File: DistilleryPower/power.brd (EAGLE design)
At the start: 50 x 86.9 mm, 68 parts, among them IC1 ACS758LCB-050B-PFF-T, IC3 MICROCHIP_BY_ELEMENT14_BATCH_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, IC4 SN65HVD230/1, J1 GREEN-2P-5.0, J2 GREEN-2P-5.0, J3 GREEN-2P-5.0, J4 GREEN-2P-5.0, J5 GREEN-2P-5.0, Q1 BC807-16LT1SMD, T1 BT138-DSH, U1 STM32F042KXTX, X1 IQD-FREQUENCY-PRODUCTS_CRYSTA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, X2 2516-

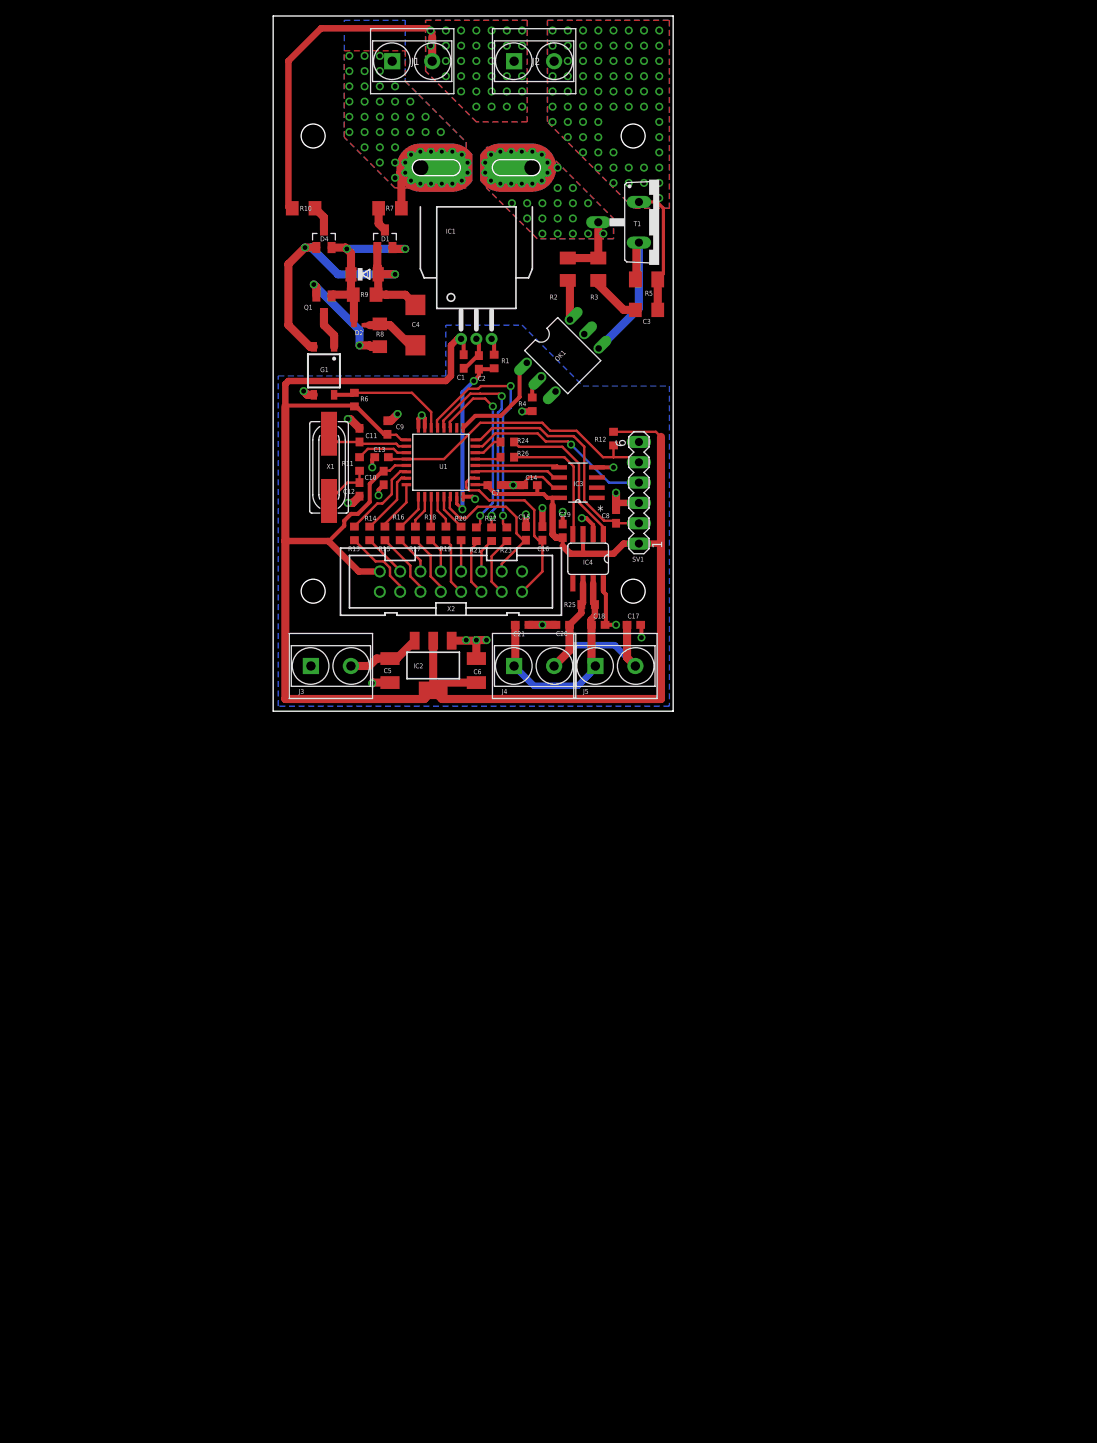
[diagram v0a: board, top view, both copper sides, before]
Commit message: reroute: indication board with CAN controller
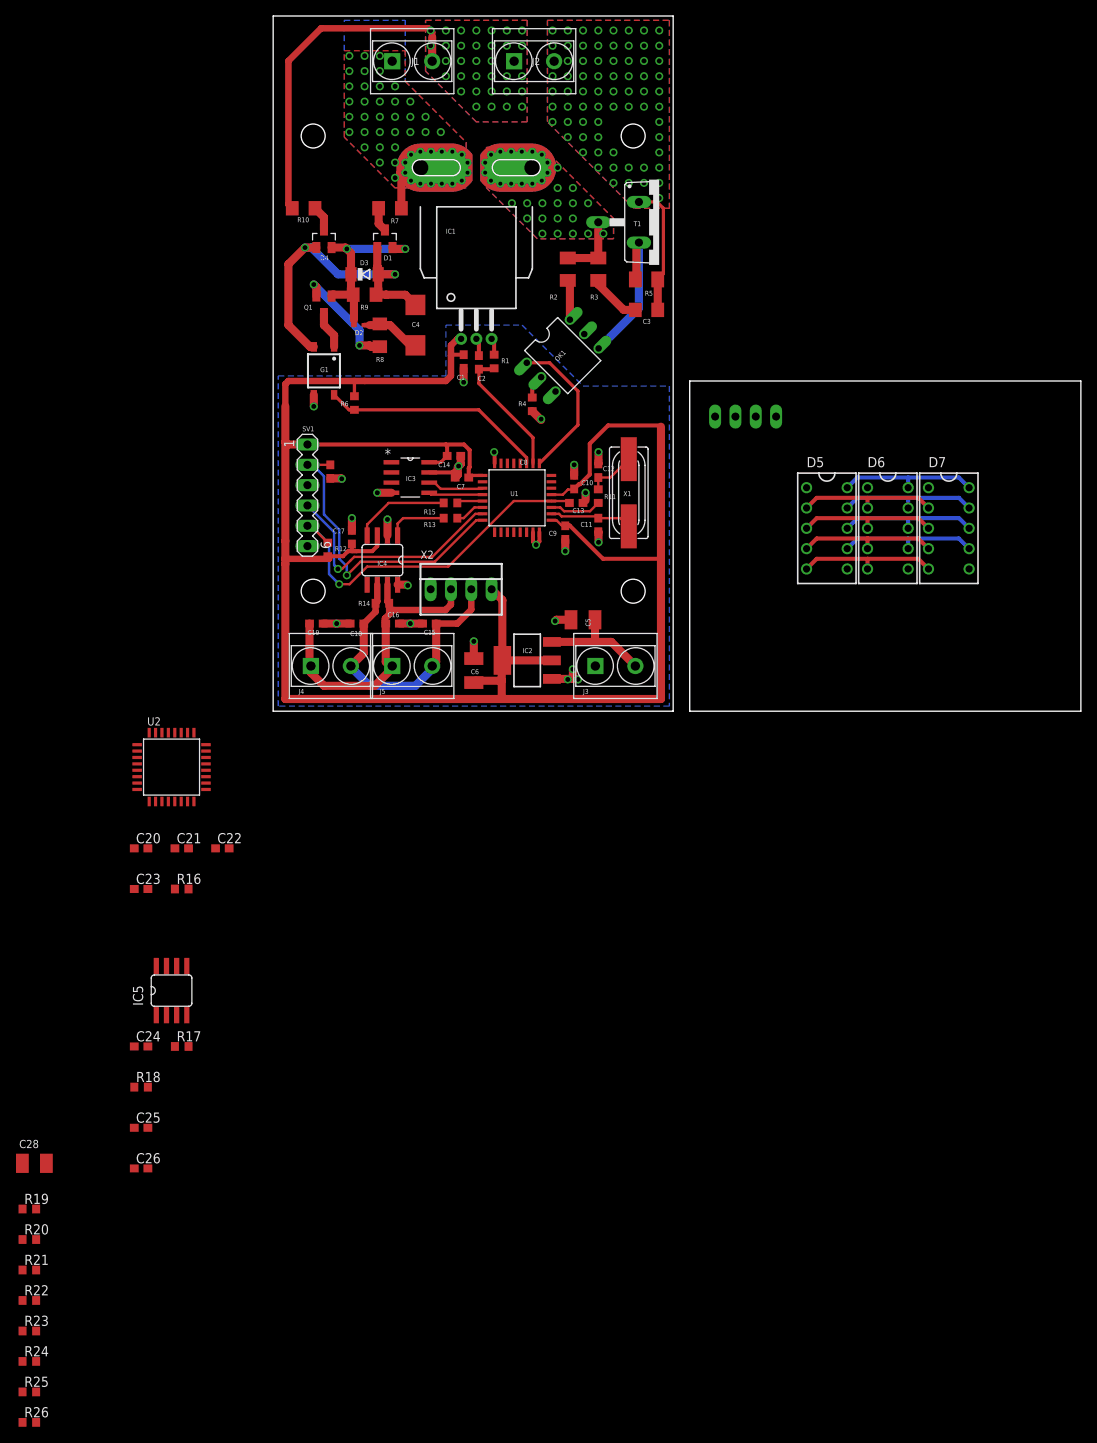
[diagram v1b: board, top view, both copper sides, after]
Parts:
- added C22, C23, C24, C25, C26: 0.1, rcl:C0603
- added C28: 10u/25, rcl:SMC_B
- added D5, D6, D7: CHRONO_LED_8X1, chrono:CHRONO_LED_DIP10
- added IC5: SN65HVD230/1, distillery:SO8
- added U2: STM32F042KXTX, stm32f0:LQFP32
- added X3: 22-23-2041, con-molex:22-23-2041
- R14: value 100 -> 120/1%
- R16, R19, R20, R21, R22, R23, R24, R26: value 100 -> (none)
- R25: value 120/1% -> (none)
- X2: value 2516- -> 22-23-2041; device con-3m:PAK100/2500-16 -> con-molex:22-23-2041
- moved R26 134.6 mm to (-30.5, -88.9), turned to 0 degrees
- moved R24 129.5 mm to (-30.5, -81.3), turned to 0 degrees
- moved R25 120.7 mm to (-30.5, -85.1)
- moved R23 116.1 mm to (-30.5, -77.5), turned to 0 degrees
- moved R22 111.9 mm to (-30.5, -73.7), turned to 0 degrees
- moved R21 107.6 mm to (-30.5, -69.8), turned to 0 degrees
- moved R20 103.5 mm to (-30.5, -66.0), turned to 0 degrees
- moved R19 99.2 mm to (-30.5, -62.2), turned to 0 degrees
- moved R18 78.1 mm to (-16.5, -47.0), turned to 0 degrees
- moved R17 70.5 mm to (-11.4, -41.9), turned to 0 degrees
- moved C20 59.7 mm to (-16.5, -17.1), turned to 0 degrees
- moved R16 52.2 mm to (-11.4, -22.2), turned to 0 degrees
- moved C21 50.9 mm to (-11.4, -17.1)
- moved SV1 41.4 mm to (4.29, 27.0), turned to 270 degrees
- moved R12 38.3 mm to (6.83, 20.2), turned to 270 degrees
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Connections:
- removed net DG0: R21.1, U1.27
- removed net DG1: R22.1, U1.28
- removed net DG2: R23.1, U1.29
- removed net N$33: R23.2, X2.13
- removed net SW0: C15.2, U1.14, X2.14
- removed net SW1: C16.2, U1.18, X2.15
- new net !I_NRST: C20.1, R16.1, U2.4
- new net I_3V3: C21.2, C22.2, C23.2, C24.2, C28.+, IC5.3, R16.2, U2.1, U2.17, U2.5, X3.4
- new net I_CAN_RX: R18.2, U2.21
- new net I_CAN_TX: R17.2, U2.22
- new net I_GND: C20.2, C21.1, C22.1, C23.1, C24.1, C25.2, C26.2, C28.-, IC5.2, IC5.8, U2.16, U2.31, U2.32, X3.1
- new net I_OSC_IN: U2.2
- new net I_OSC_OUT: U2.3
- new net LED_1: D5.1, D5.6
- new net LED_2: D6.1, D6.6
- new net LED_3: D7.1, D7.6
- new net N$12: C25.1, IC5.6, X3.3
- new net N$19: IC5.4, R18.1
- net +3V3: now also C17.2, X2.4; no longer C19.2, X2.2
- net A: now also D5.10, D6.10, D7.10, R19.1; no longer R13.1, U1.6
- net B: now also D5.9, D6.9, D7.9, R20.1; no longer R14.1, U1.7
- net C: now also D5.8, D6.8, D7.8, R21.1; no longer R15.1, U1.8
- net CAN_RX: now also R15.2; no longer R26.2
- net CAN_TX: now also R13.2; no longer R24.2
- net CUR_LOAD: now also U1.10; no longer U1.15
- net D: now also D5.5, D6.5, D7.5, R22.1; no longer R16.1, U1.9
- net DP: now also D5.7, D6.7, D7.7, R26.1; no longer R20.1, U1.13
- net E: now also D5.4, D6.4, D7.4, R23.1; no longer R17.1, U1.10
- net F: now also D5.2, D6.2, D7.2, R24.1; no longer R18.1, U1.11
- net G: now also D5.3, D6.3, D7.3, R25.1; no longer R19.1, U1.12
- net GND: now also C15.2, C16.2, C17.1, C19.2; no longer C15.1, C16.1, C17.2, C19.1, C20.2, C21.2, X2.16
- net N$15: now also IC5.1, R17.1; no longer R13.2, X2.3
- net N$20: now also C15.1, C18.1, R14.1, X2.3; no longer C17.1, C20.1, R25.1
- net N$21: now also R13.1; no longer R24.1
- net N$22: now also R15.1; no longer R26.1
- net N$23: now also C26.1, IC5.7, X3.2; no longer R14.2, X2.4
- net N$24: now also C16.1, C19.1, R14.2, X2.2; no longer C18.1, C21.1, R25.2
- net N$25: now also R19.2, U2.6; no longer R15.2, X2.5
- net N$26: now also R20.2, U2.7; no longer R16.2, X2.6
- net N$27: now also R21.2, U2.8; no longer R17.2, X2.7
- net N$28: now also R22.2, U2.9; no longer R18.2, X2.8
- net N$29: now also R23.2, U2.10; no longer R19.2, X2.9
- net N$30: now also R24.2, U2.11; no longer R20.2, X2.10
- net N$31: now also R25.2, U2.12; no longer R21.2, X2.11
- net N$32: now also R26.2, U2.13; no longer R22.2, X2.12
- net PHASE_OUT: now also U1.9; no longer U1.25
- net ZERO_CROSS: now also U1.11; no longer U1.30
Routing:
- net DG2: track 30.2 -> 0.00 mm, vias 2 -> 0
- net DG1: track 26.7 -> 0.00 mm, vias 2 -> 0
- net DG0: track 23.7 -> 0.00 mm, vias 2 -> 0
- net SW1: track 23.7 -> 0.00 mm
- net SW0: track 20.2 -> 0.00 mm
- net GND: track 66.2 -> 49.1 mm
- net F: track 3.77 -> 17.6 mm
- net G: track 4.17 -> 17.6 mm
- net E: track 4.23 -> 17.6 mm
- net DP: track 4.63 -> 17.6 mm
- net ZERO_CROSS: track 15.2 -> 28.0 mm
- net D: track 4.76 -> 17.6 mm
- net N$21: track 19.3 -> 7.53 mm
- net C: track 6.35 -> 17.6 mm
- net N$24: track 28.7 -> 39.5 mm
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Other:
- board size 50 x 86.9 mm -> 101 x 86.9 mm

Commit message: indication board routing finished
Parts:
- added C27: 100p, rcl:C0603
- added C29, C30: 20p, rcl:C0603
- added R27, R28, R29: 10k, rcl:R0603
- added R30: 220, rcl:R0603
- added S1, S2: SWITCH-TACT_DTS-6, chrono:SWITCH-TACT_DTS-6
- added SV2: (no value), distillery:CON-LSTB_MA06-1
- added VT1, VT2, VT3: WALKGEEK-EAGLE_IRLML6402, chrono:WALKGEEK-EAGLE_MICRO3
- added X4: IQD-FREQUENCY-PRODUCTS_CRYSTALS-NOGND-4-HSMX, distillery:IQD-FREQUENCY-PRODUCTS_HC49-4-HSMX
- moved R26 171.5 mm to (91.4, 31.8)
- moved R25 165.7 mm to (88.3, 30.5)
- moved R24 164.5 mm to (91.4, 29.2)
- moved R21 158.8 mm to (88.3, 35.6)
- moved R23 158.8 mm to (88.3, 27.9)
- moved R20 157.9 mm to (91.4, 34.3)
- moved R22 157.9 mm to (91.4, 26.7)
- moved R19 152.2 mm to (88.3, 33.0)
- moved C28 127.6 mm to (56.5, 37.5)
- moved C26 114.8 mm to (59.1, 29.2)
- moved C20 113.4 mm to (92.7, 13.3), turned to 180 degrees
- moved C25 112.9 mm to (59.1, 31.8)
- moved R16 109.4 mm to (92.7, 11.4), turned to 180 degrees
- moved R18 99.2 mm to (64.1, 10.8)
- moved C24 95.0 mm to (61.3, 12.5), turned to 180 degrees
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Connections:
- removed net LED_1: D5.1, D5.6
- removed net LED_2: D6.1, D6.6
- removed net LED_3: D7.1, D7.6
- new net AN_LED_1: D5.6, VT1.3
- new net AN_LED_2: D6.6, VT2.3
- new net AN_LED_3: D7.6, VT3.3
- new net BTN_1: S2.3, S2.4, U2.8
- new net BTN_2: S1.3, S1.4, U2.19
- new net I_SWCLK: C27.2, SV2.2, U2.24
- new net I_SWDIO: SV2.4, U2.23
- new net N$33: C30.2, R30.1, X4.2
- new net P_LED_1: R27.2, U2.28, VT1.1
- new net P_LED_2: R28.2, U2.29, VT2.1
- new net P_LED_3: R29.2, U2.30, VT3.1
- net !I_NRST: now also SV2.5
- net A: now also R21.1; no longer R19.1
- net B: now also R19.1; no longer R20.1
- net C: now also R25.1; no longer R21.1
- net DP: now also R23.1; no longer R26.1
- net E: now also R24.1; no longer R23.1
- net F: now also R20.1; no longer R24.1
- net G: now also R26.1; no longer R25.1
- net I_3V3: now also R27.1, R28.1, R29.1, SV2.1, VT1.2, VT2.2, VT3.2
- net I_GND: now also C27.1, C29.1, C30.1, S1.1, S1.2, S2.1, S2.2, SV2.3
- net I_OSC_IN: now also C29.2, X4.1
- net I_OSC_OUT: now also R30.2
- net N$25: now also U2.14; no longer U2.6
- net N$26: now also U2.15; no longer U2.7
- net N$27: now also U2.18; no longer U2.8
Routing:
- net I_3V3: track 0.00 -> 185.3 mm
- net I_SWDIO: track 0.00 -> 47.2 mm, vias 0 -> 2
- net N$27: track 0.00 -> 46.4 mm, vias 0 -> 2
- net I_SWCLK: track 0.00 -> 45.1 mm, vias 0 -> 2
- net N$26: track 0.00 -> 38.2 mm, vias 0 -> 2
- net N$25: track 0.00 -> 37.9 mm, vias 0 -> 2
- net N$31: track 0.00 -> 37.0 mm, vias 0 -> 2
- net I_GND: track 0.00 -> 35.4 mm, vias 0 -> 14
- net P_LED_3: track 0.00 -> 34.5 mm, vias 0 -> 2
- net N$32: track 0.00 -> 34.2 mm, vias 0 -> 2
- net BTN_1: track 0.00 -> 33.8 mm, vias 0 -> 2
- net N$29: track 0.00 -> 33.5 mm, vias 0 -> 2
- net N$30: track 0.00 -> 33.4 mm, vias 0 -> 2
- net !I_NRST: track 0.00 -> 32.5 mm, vias 0 -> 1
- net N$12: track 0.00 -> 30.7 mm, vias 0 -> 1
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- added copper zone on layer 16, net I_GND
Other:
- board size 101 x 86.9 mm -> 99.1 x 86.9 mm

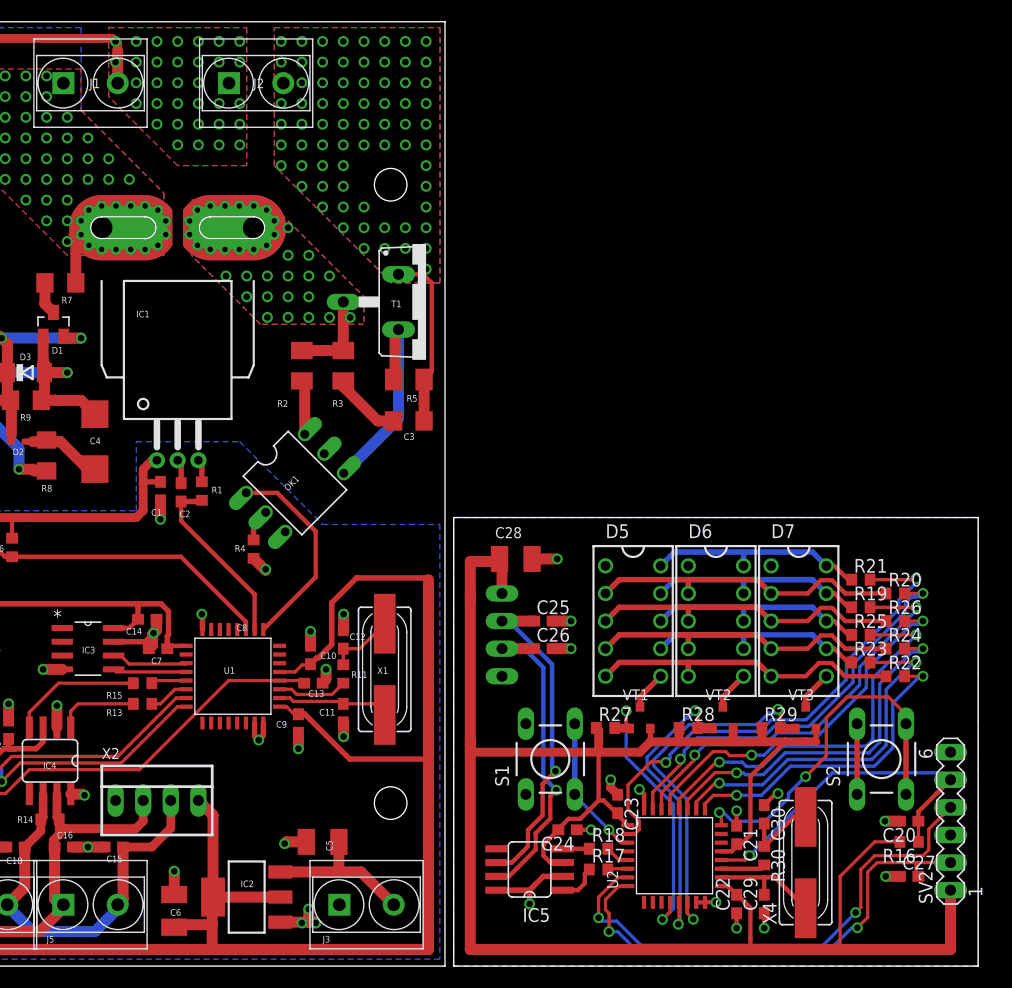
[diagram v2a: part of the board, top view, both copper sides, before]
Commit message: added 1wire; finished profile layer
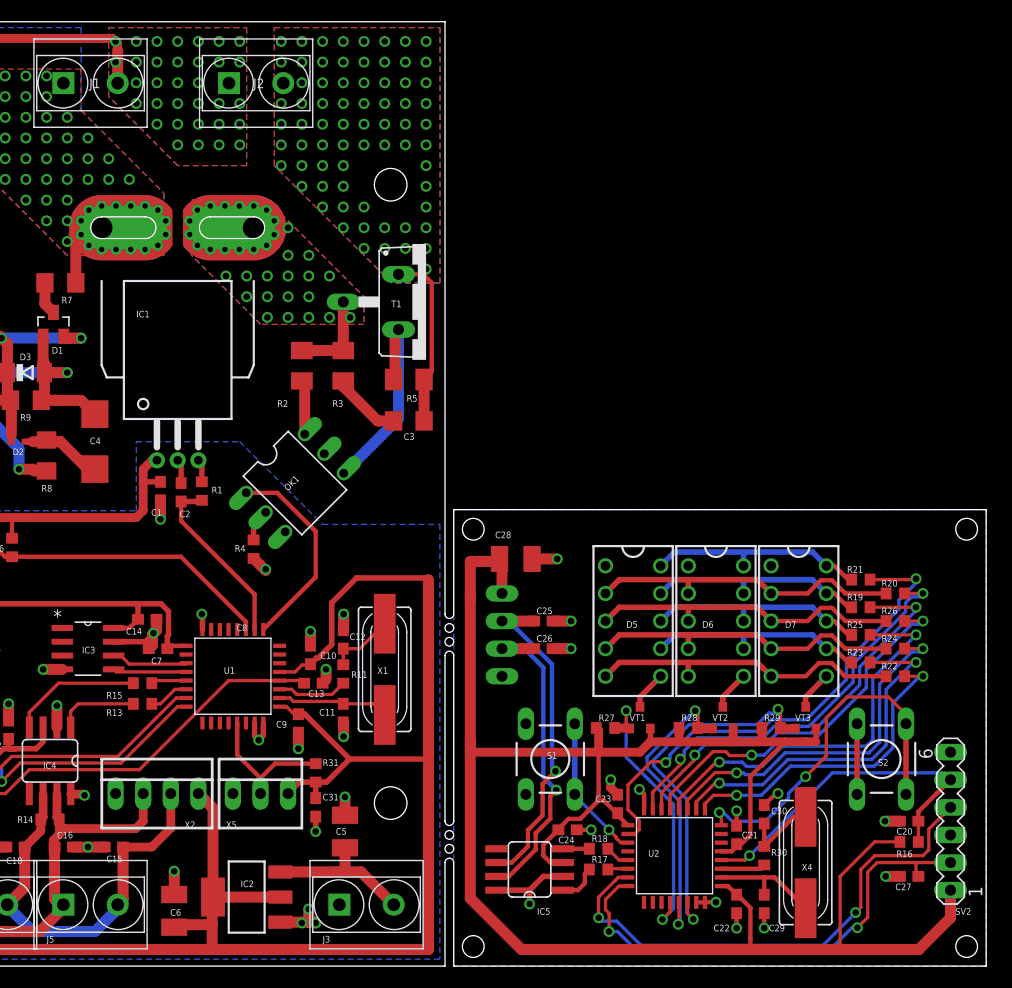
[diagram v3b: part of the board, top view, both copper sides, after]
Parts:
- added C31: 0.1, rcl:C0603
- added R31: 4k7, rcl:R0603
- added X5: 22-23-2031, con-molex:22-23-2031
- moved C5 2.27 mm to (40.8, 12.4), turned to 90 degrees
- moved X2 0.63 mm to (23.5, 15.9)
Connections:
- new net 1WIRE: R31.1, U1.29, X5.2
- net +3V3: now also C31.1, R31.2, X5.3
- net GND: now also C31.2, X5.1
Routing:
- net 1WIRE: track 0.00 -> 13.0 mm
- net +3V3: track 258.2 -> 267.3 mm
- net I_3V3: track 185.3 -> 180.8 mm
- net GND: track 49.1 -> 50.1 mm, vias 23 -> 24
- net !I_NRST: track 32.5 -> 31.6 mm
- net N$13: track 14.5 -> 13.9 mm
- net N$20: track 37.2 -> 37.8 mm
- net N$24: track 39.5 -> 40.2 mm
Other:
- board size 99.1 x 86.9 mm -> 99.8 x 86.9 mm

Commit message: fixed profile
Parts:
- moved SV2 36.5 mm to (79.7, 45.7), turned to 180 degrees
- moved C27 34.6 mm to (84.7, 41.9), turned to 90 degrees
- moved R20 33.3 mm to (58.7, 40.6), turned to 90 degrees
- moved R16 32.5 mm to (81.6, 41.9), turned to 270 degrees
- moved C28 31.8 mm to (55.5, 5.71), turned to 90 degrees
- moved R26 31.5 mm to (61.2, 40.6), turned to 90 degrees
- moved C20 31.4 mm to (79.7, 41.9), turned to 270 degrees
- moved R21 30.9 mm to (57.4, 37.5), turned to 90 degrees
- moved R24 29.9 mm to (63.8, 40.6), turned to 90 degrees
- moved R22 28.7 mm to (66.3, 40.6), turned to 90 degrees
- moved R19 28.6 mm to (60.0, 37.5), turned to 90 degrees
- moved X3 27.0 mm to (62.5, 4.45), turned to 0 degrees
- moved R25 26.7 mm to (62.5, 37.5), turned to 90 degrees
- moved IC5 26.4 mm to (84.1, 6.99), turned to 180 degrees
- moved S2 26.0 mm to (74.0, 39.4), turned to 180 degrees
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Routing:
- net I_3V3: track 180.8 -> 180.2 mm
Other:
- board size 99.8 x 86.9 mm -> 93 x 86.9 mm
